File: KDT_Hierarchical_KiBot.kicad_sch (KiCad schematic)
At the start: 0 parts

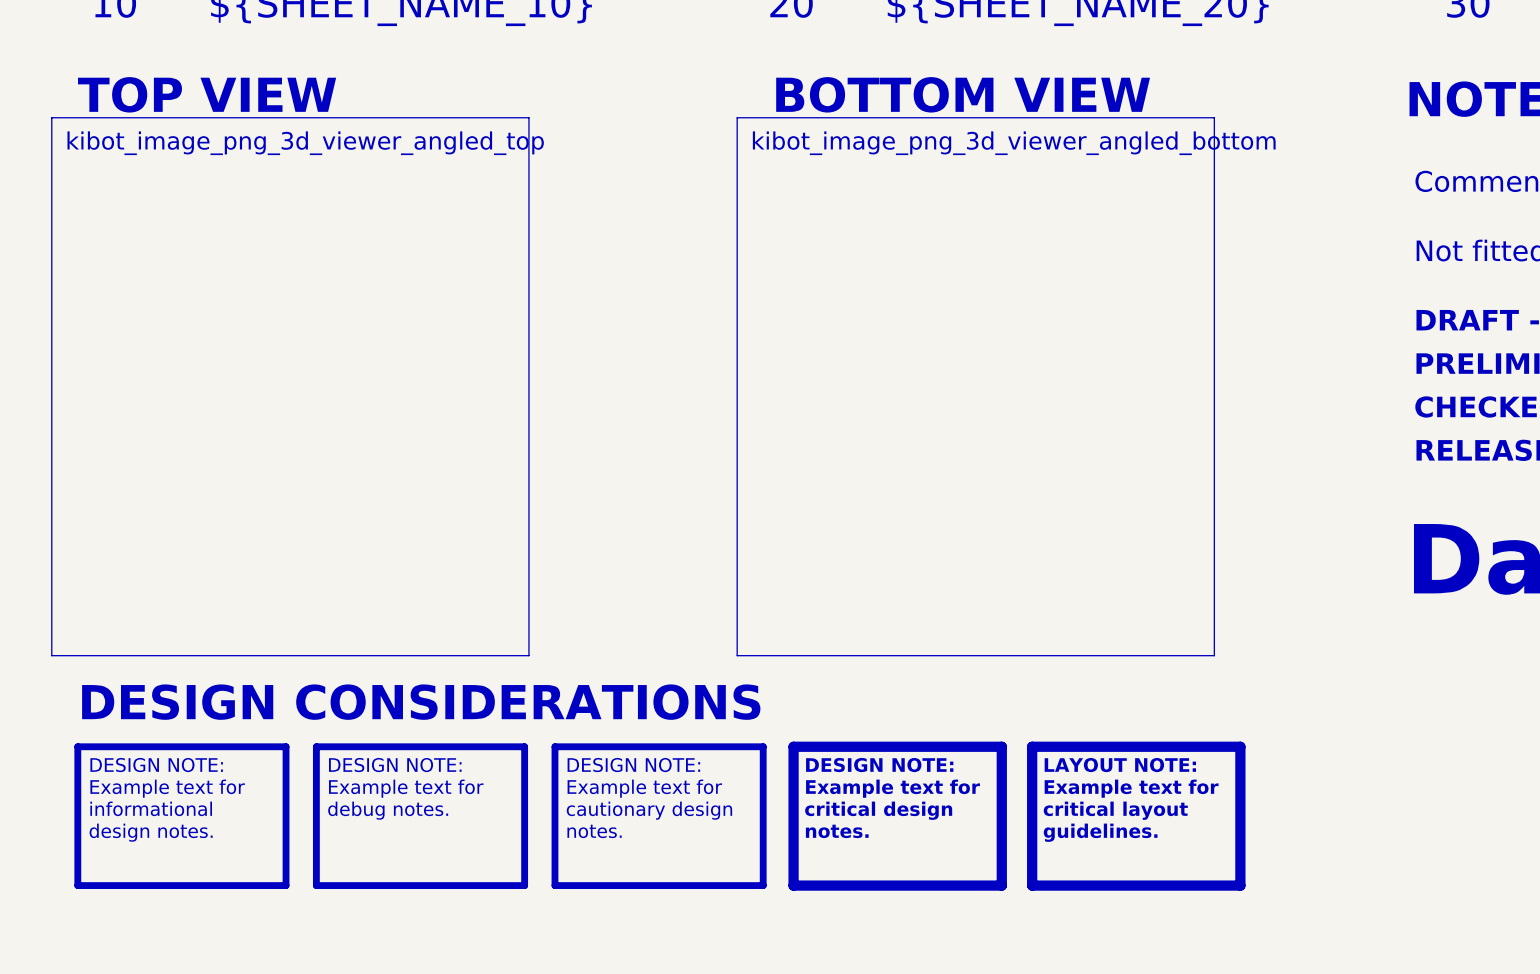
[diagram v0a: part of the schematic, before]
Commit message: customise for 2 layer
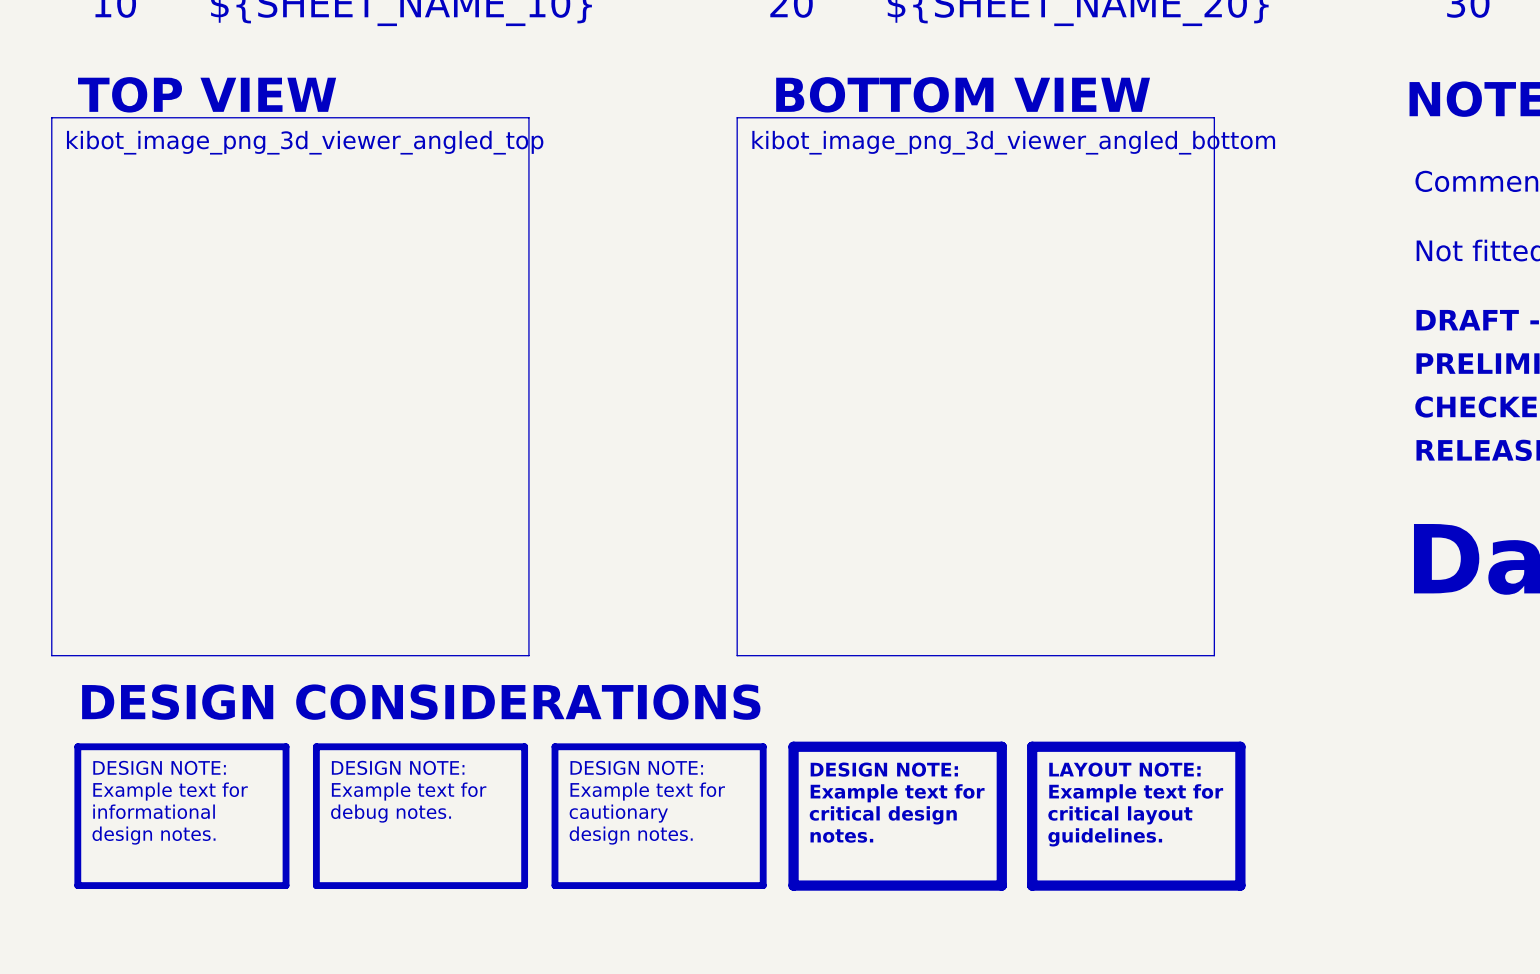
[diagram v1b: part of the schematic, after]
